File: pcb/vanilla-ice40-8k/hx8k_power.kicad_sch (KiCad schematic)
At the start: 37 parts, among them U1 ICE40HX8K-CT256

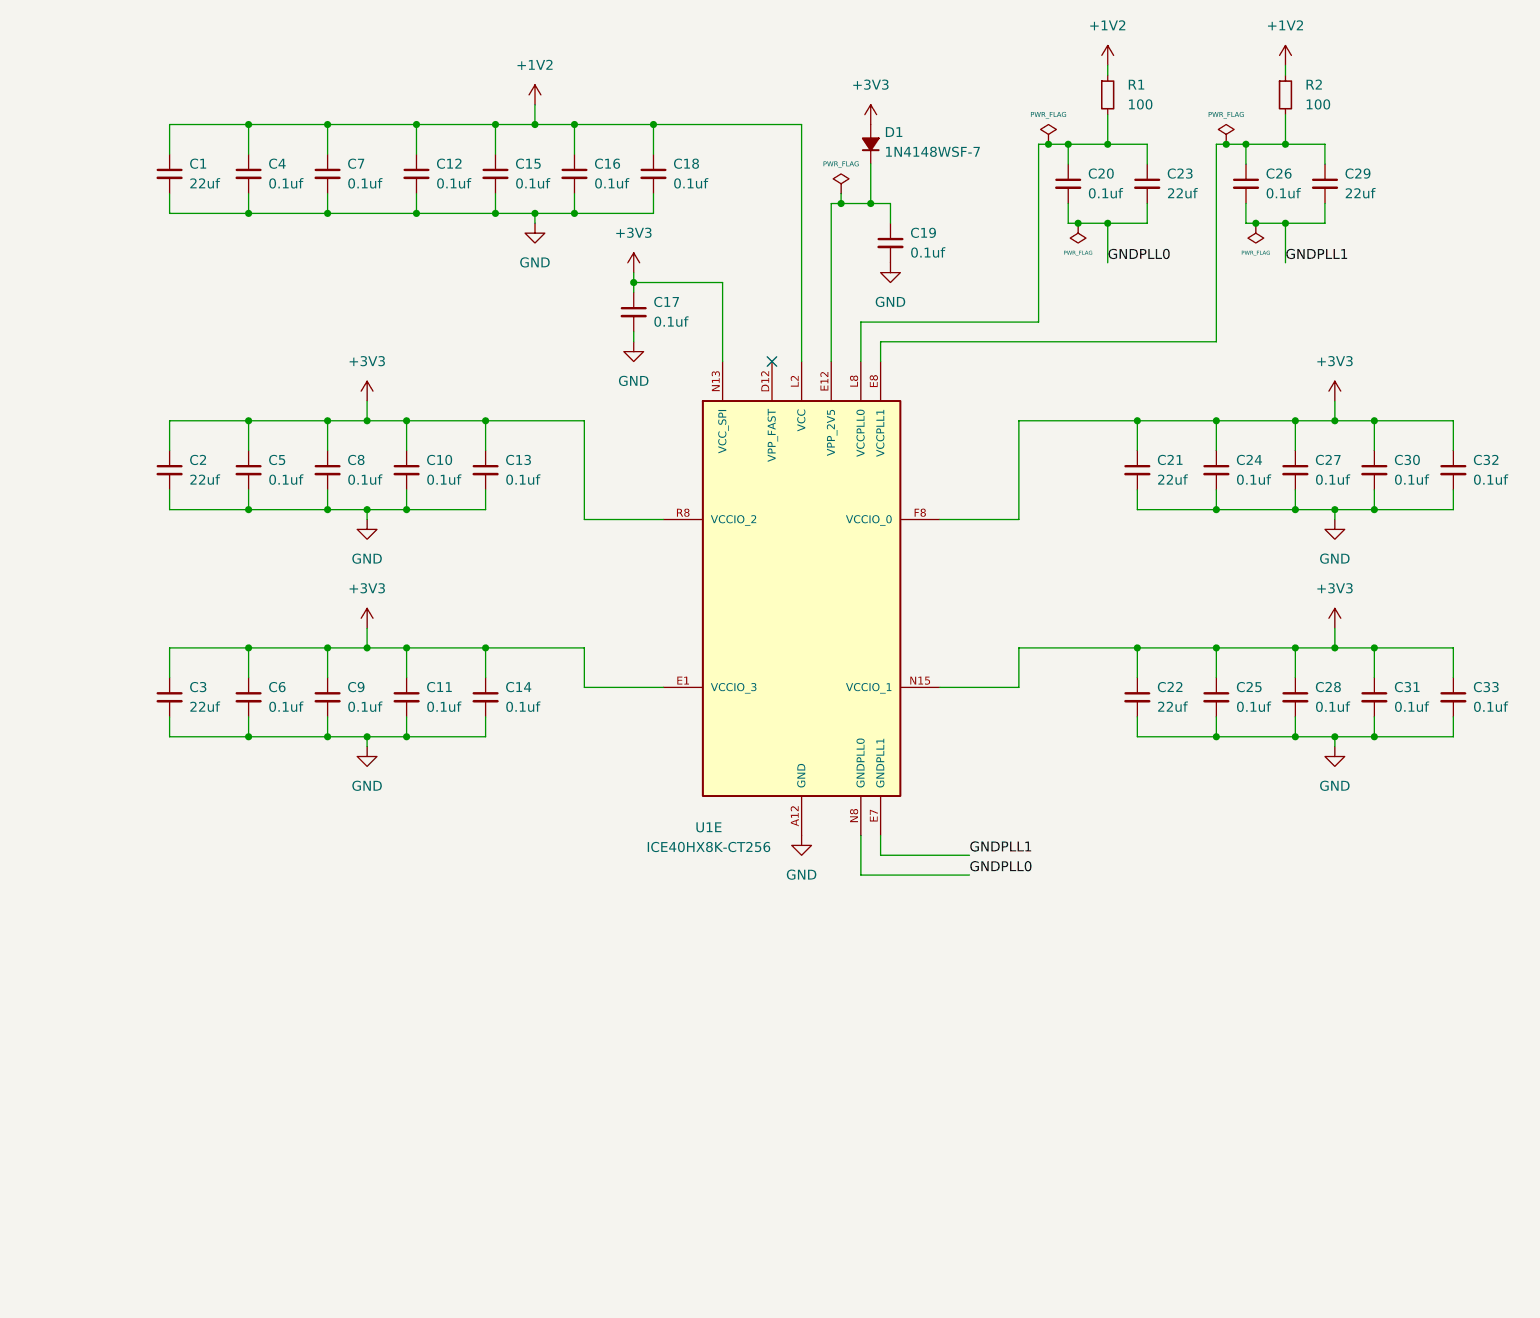
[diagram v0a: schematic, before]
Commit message: [pcb][hx8k] redid components with vip
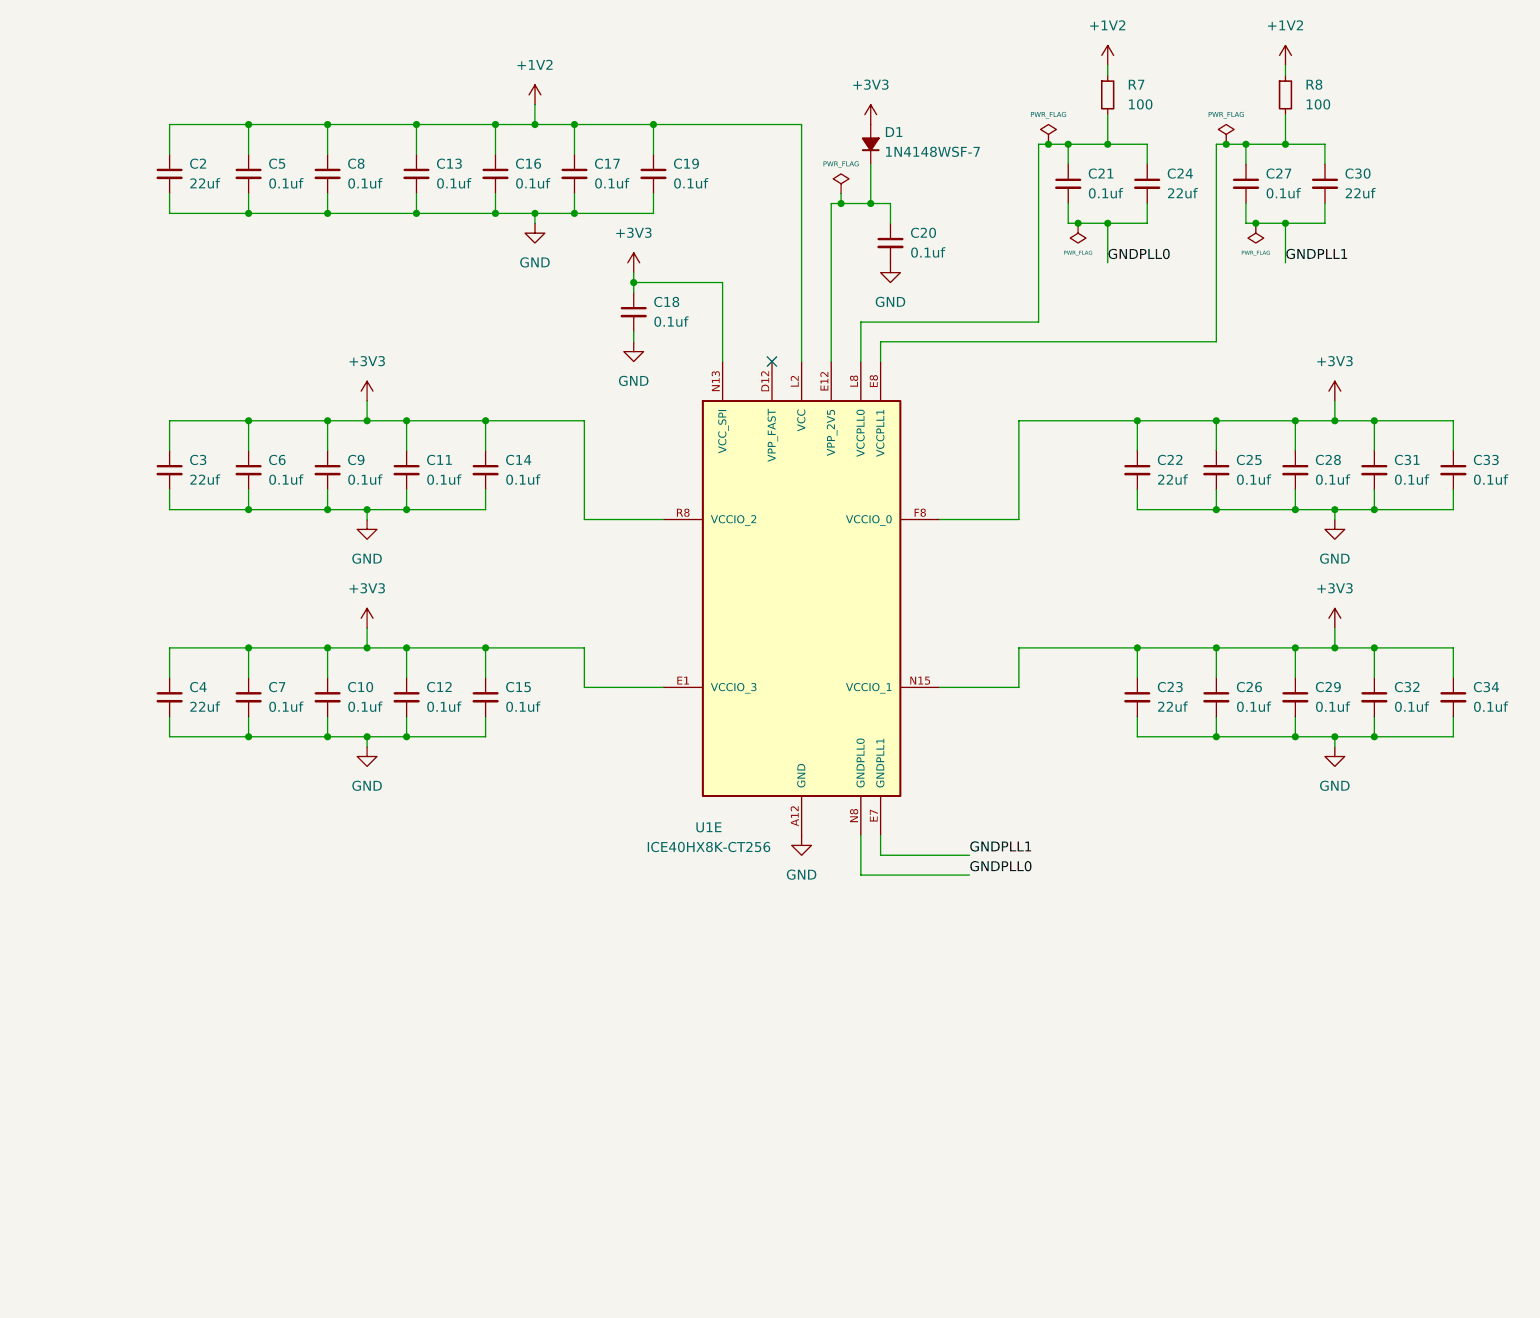
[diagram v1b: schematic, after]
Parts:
- renumbered C9 to C10, C10 to C11, C11 to C12, C12 to C13, C13 to C14, C14 to C15, C15 to C16, C16 to C17, C17 to C18, C18 to C19, C1 to C2, C19 to C20, C20 to C21, C21 to C22, C22 to C23, C23 to C24, C24 to C25, C25 to C26, C26 to C27, C27 to C28, C28 to C29, C2 to C3, C29 to C30, C30 to C31, C31 to C32, C32 to C33, C33 to C34, C3 to C4, C4 to C5, C5 to C6, C6 to C7, C7 to C8, C8 to C9, R1 to R7, R2 to R8

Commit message: [pcb][hx8k] rerouted; all pins done
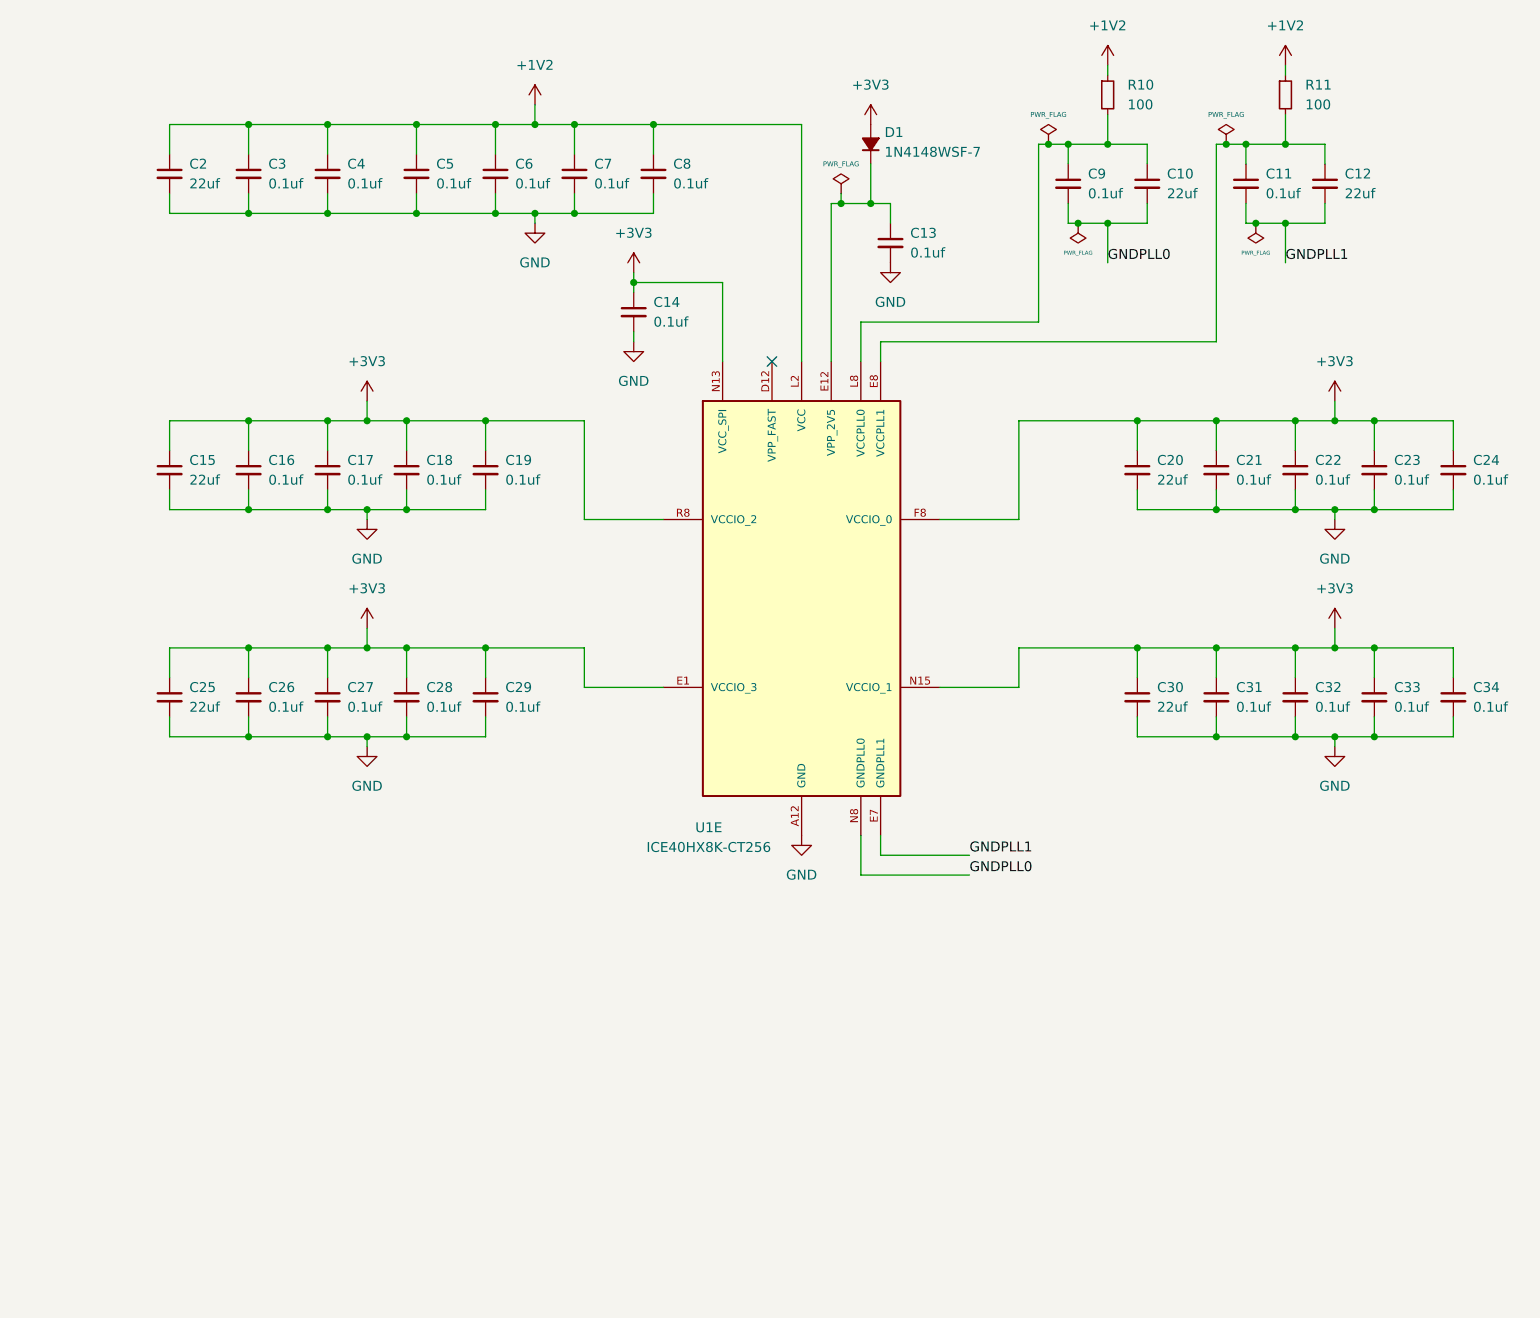
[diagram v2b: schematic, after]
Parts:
- C11: renamed from C27; footprint custom:C_0402_1005Metric_no_courtyard -> Capacitor_SMD:C_0201_0603Metric; Digi-Key Part Number 490-6328-1-ND -> (none); LCSC Part # C1525 -> (none)
- C13: renamed from C20; footprint custom:C_0402_1005Metric_no_courtyard -> Capacitor_SMD:C_0201_0603Metric; Digi-Key Part Number 490-6328-1-ND -> (none); LCSC Part # C1525 -> (none)
- C14: renamed from C18; footprint custom:C_0402_1005Metric_no_courtyard -> Capacitor_SMD:C_0201_0603Metric; Digi-Key Part Number 490-6328-1-ND -> (none); LCSC Part # C1525 -> (none)
- C16: renamed from C6; footprint custom:C_0402_1005Metric_no_courtyard -> Capacitor_SMD:C_0201_0603Metric; Digi-Key Part Number 490-6328-1-ND -> (none); LCSC Part # C1525 -> (none)
- C17: renamed from C9; footprint custom:C_0402_1005Metric_no_courtyard -> Capacitor_SMD:C_0201_0603Metric; Digi-Key Part Number 490-6328-1-ND -> (none); LCSC Part # C1525 -> (none)
- C18: renamed from C11; footprint custom:C_0402_1005Metric_no_courtyard -> Capacitor_SMD:C_0201_0603Metric; Digi-Key Part Number 490-6328-1-ND -> (none); LCSC Part # C1525 -> (none)
- C19: renamed from C14; footprint custom:C_0402_1005Metric_no_courtyard -> Capacitor_SMD:C_0201_0603Metric; Digi-Key Part Number 490-6328-1-ND -> (none); LCSC Part # C1525 -> (none)
- C21: renamed from C25; footprint custom:C_0402_1005Metric_no_courtyard -> Capacitor_SMD:C_0201_0603Metric; Digi-Key Part Number 490-6328-1-ND -> (none); LCSC Part # C1525 -> (none)
- C22: renamed from C28; footprint custom:C_0402_1005Metric_no_courtyard -> Capacitor_SMD:C_0201_0603Metric; Digi-Key Part Number 490-6328-1-ND -> (none); LCSC Part # C1525 -> (none)
- C23: renamed from C31; footprint custom:C_0402_1005Metric_no_courtyard -> Capacitor_SMD:C_0201_0603Metric; Digi-Key Part Number 490-6328-1-ND -> (none); LCSC Part # C1525 -> (none)
- C24: renamed from C33; footprint custom:C_0402_1005Metric_no_courtyard -> Capacitor_SMD:C_0201_0603Metric; Digi-Key Part Number 490-6328-1-ND -> (none); LCSC Part # C1525 -> (none)
- C26: renamed from C7; footprint custom:C_0402_1005Metric_no_courtyard -> Capacitor_SMD:C_0201_0603Metric; Digi-Key Part Number 490-6328-1-ND -> (none); LCSC Part # C1525 -> (none)
- C27: renamed from C10; footprint custom:C_0402_1005Metric_no_courtyard -> Capacitor_SMD:C_0201_0603Metric; Digi-Key Part Number 490-6328-1-ND -> (none); LCSC Part # C1525 -> (none)
- C28: renamed from C12; footprint custom:C_0402_1005Metric_no_courtyard -> Capacitor_SMD:C_0201_0603Metric; Digi-Key Part Number 490-6328-1-ND -> (none); LCSC Part # C1525 -> (none)
- C29: renamed from C15; footprint custom:C_0402_1005Metric_no_courtyard -> Capacitor_SMD:C_0201_0603Metric; Digi-Key Part Number 490-6328-1-ND -> (none); LCSC Part # C1525 -> (none)
- C3: renamed from C5; footprint custom:C_0402_1005Metric_no_courtyard -> Capacitor_SMD:C_0201_0603Metric; Digi-Key Part Number 490-6328-1-ND -> (none); LCSC Part # C1525 -> (none)
- C31: renamed from C26; footprint custom:C_0402_1005Metric_no_courtyard -> Capacitor_SMD:C_0201_0603Metric; Digi-Key Part Number 490-6328-1-ND -> (none); LCSC Part # C1525 -> (none)
- C32: renamed from C29; footprint custom:C_0402_1005Metric_no_courtyard -> Capacitor_SMD:C_0201_0603Metric; Digi-Key Part Number 490-6328-1-ND -> (none); LCSC Part # C1525 -> (none)
- C33: renamed from C32; footprint custom:C_0402_1005Metric_no_courtyard -> Capacitor_SMD:C_0201_0603Metric; Digi-Key Part Number 490-6328-1-ND -> (none); LCSC Part # C1525 -> (none)
- C34: footprint custom:C_0402_1005Metric_no_courtyard -> Capacitor_SMD:C_0201_0603Metric; Digi-Key Part Number 490-6328-1-ND -> (none); LCSC Part # C1525 -> (none)
- C4: renamed from C8; footprint custom:C_0402_1005Metric_no_courtyard -> Capacitor_SMD:C_0201_0603Metric; Digi-Key Part Number 490-6328-1-ND -> (none); LCSC Part # C1525 -> (none)
- C5: renamed from C13; footprint custom:C_0402_1005Metric_no_courtyard -> Capacitor_SMD:C_0201_0603Metric; Digi-Key Part Number 490-6328-1-ND -> (none); LCSC Part # C1525 -> (none)
- C6: renamed from C16; footprint custom:C_0402_1005Metric_no_courtyard -> Capacitor_SMD:C_0201_0603Metric; Digi-Key Part Number 490-6328-1-ND -> (none); LCSC Part # C1525 -> (none)
- C7: renamed from C17; footprint custom:C_0402_1005Metric_no_courtyard -> Capacitor_SMD:C_0201_0603Metric; Digi-Key Part Number 490-6328-1-ND -> (none); LCSC Part # C1525 -> (none)
- C8: renamed from C19; footprint custom:C_0402_1005Metric_no_courtyard -> Capacitor_SMD:C_0201_0603Metric; Digi-Key Part Number 490-6328-1-ND -> (none); LCSC Part # C1525 -> (none)
- C9: renamed from C21; footprint custom:C_0402_1005Metric_no_courtyard -> Capacitor_SMD:C_0201_0603Metric; Digi-Key Part Number 490-6328-1-ND -> (none); LCSC Part # C1525 -> (none)
- renumbered C24 to C10, C30 to C12, C3 to C15, C22 to C20, C4 to C25, C23 to C30, R7 to R10, R8 to R11
